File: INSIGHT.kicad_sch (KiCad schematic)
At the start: 22 parts, among them J1 HX711 AMP 2, J10 Rest Switch, J11 Motor, J12 Load Cell 1, J13 Load Cell 2, J14 E-Stop 1, J2 HX711 AMP 1, J3 Power In, J4 Power Switch, J5 E-Stop 2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

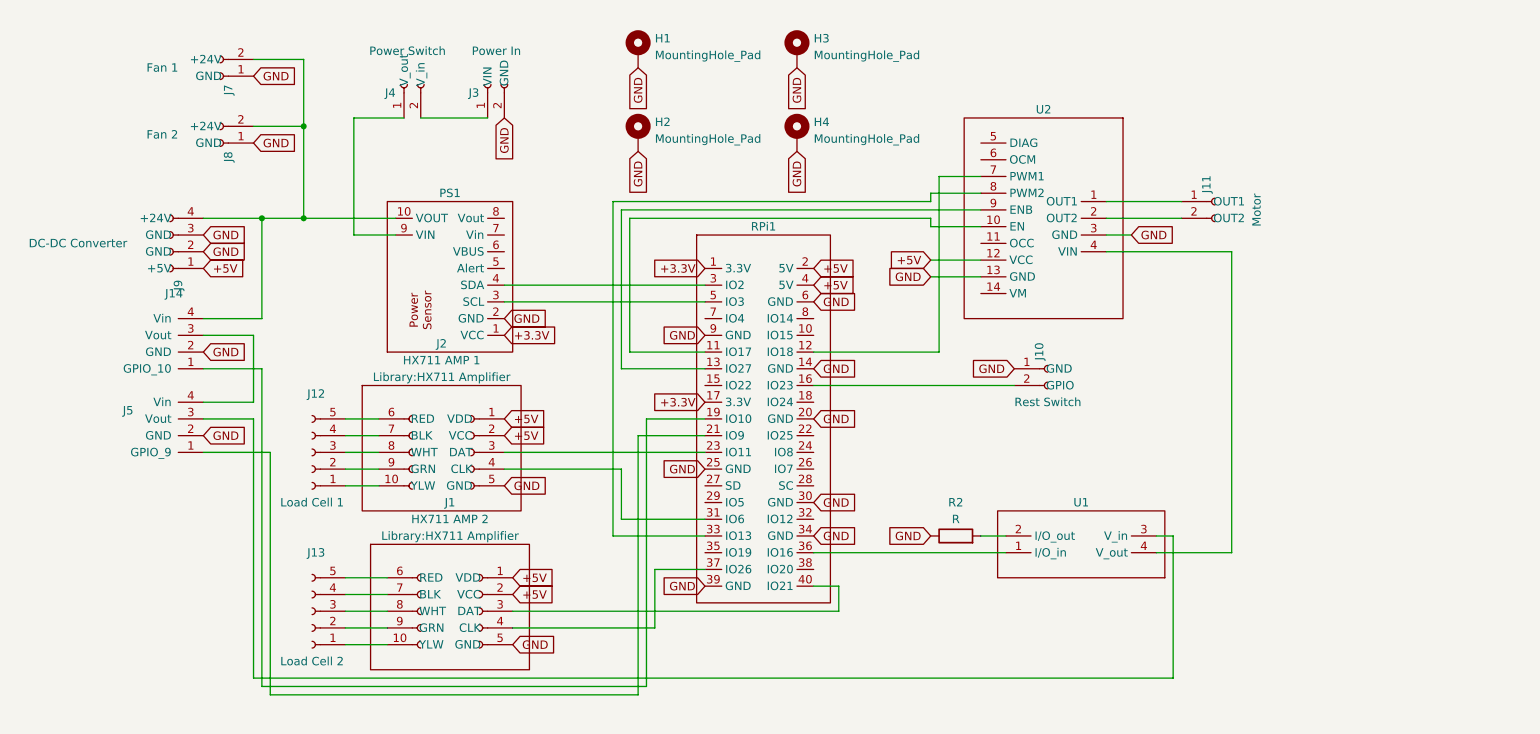
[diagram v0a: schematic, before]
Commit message: New schematic
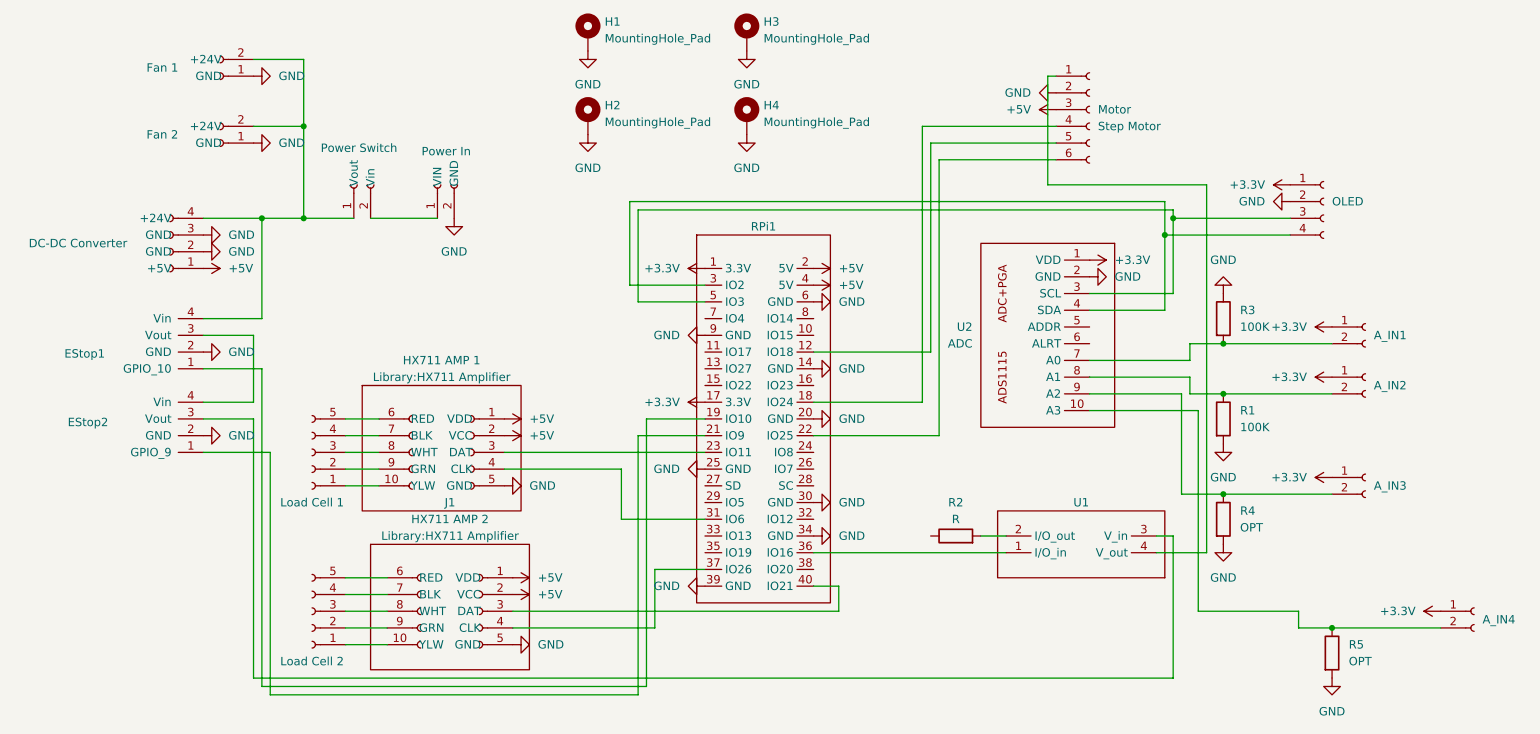
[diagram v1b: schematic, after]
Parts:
- removed J10: Rest Switch, Connector_PinSocket_2.54mm:PinSocket_1x02_P2.54mm_Vertical, symbol Connector:Conn_01x02_Socket
- removed J11: Motor, Connector_PinSocket_2.54mm:PinSocket_1x02_P2.54mm_Vertical, symbol Connector:Conn_01x02_Socket
- removed PS1: ~, Library:Power Sensor, symbol INSIGHT_Library:Power_Sensor
- removed U2: ~, Library:Motor_Driver, symbol INSIGHT_Library:Motor_Driver
- added A_IN1, A_IN2, A_IN3, A_IN4: Conn_01x02_Socket, symbol Connector:Conn_01x02_Socket
- added Motor: Step Motor, symbol Connector:Conn_01x06_Socket
- added OLED: Conn_01x04_Socket, symbol Connector:Conn_01x04_Socket
- added R1, R3: 100K, symbol Device:R
- added R4, R5: OPT, symbol Device:R
- added U2: ADC, symbol Custom_Library:ADS1115_module
- renumbered J14 to EStop1, J5 to EStop2
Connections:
- net +3.3V: now also A_IN1.1 (Pin_1), A_IN2.1 (Pin_1), A_IN3.1 (Pin_1), A_IN4.1 (Pin_1), OLED.1 (Pin_1), U2.1 (VDD)
- net +5V: now also Motor.3 (Pin_3)
- net GND: now also Motor.2 (Pin_2), OLED.2 (Pin_2), R1.2, R3.1, R4.2, R5.2, U2.2 (GND); no longer R2.1
- net at EStop1.4 (Vin), J7.2 (+24V), J8.2 (+24V)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: now also J4.1 (Vout)
- net at U1.4 (V_out): now also Motor.1 (Pin_1)
- net at RPi1.12 (IO18): now also Motor.5 (Pin_5)
- net at RPi1.18 (IO24): now also Motor.4 (Pin_4)
- net at RPi1.22 (IO25): now also Motor.6 (Pin_6)
- net at RPi1.3 (IO2): now also OLED.4 (Pin_4), U2.4 (SDA)
- net at RPi1.5 (IO3): now also OLED.3 (Pin_3), U2.3 (SCL)
- new net: A_IN1.2 (Pin_2), R3.2, U2.7 (A0)
- new net: A_IN3.2 (Pin_2), R4.1, U2.9 (A2)
- new net: A_IN4.2 (Pin_2), R5.1, U2.10 (A3)
- new net: A_IN2.2 (Pin_2), R1.1, U2.8 (A1)
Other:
- moved on the sheet: H1, H2, H3, H4
